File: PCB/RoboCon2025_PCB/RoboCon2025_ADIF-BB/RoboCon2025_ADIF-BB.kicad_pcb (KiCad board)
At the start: 2 copper layers, 47 x 72 mm, 27 parts, among them J1 Conn_01x05, J2 Conn_01x09, J3 Conn_01x09, J4 S2B-XH-A, J6 S3B-XH-A, J7 S2B-XH-A, J8 S2B-XH-A, J9 S3B-XH-A, U1 PCM5102A, U3 TBD62083AFNG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

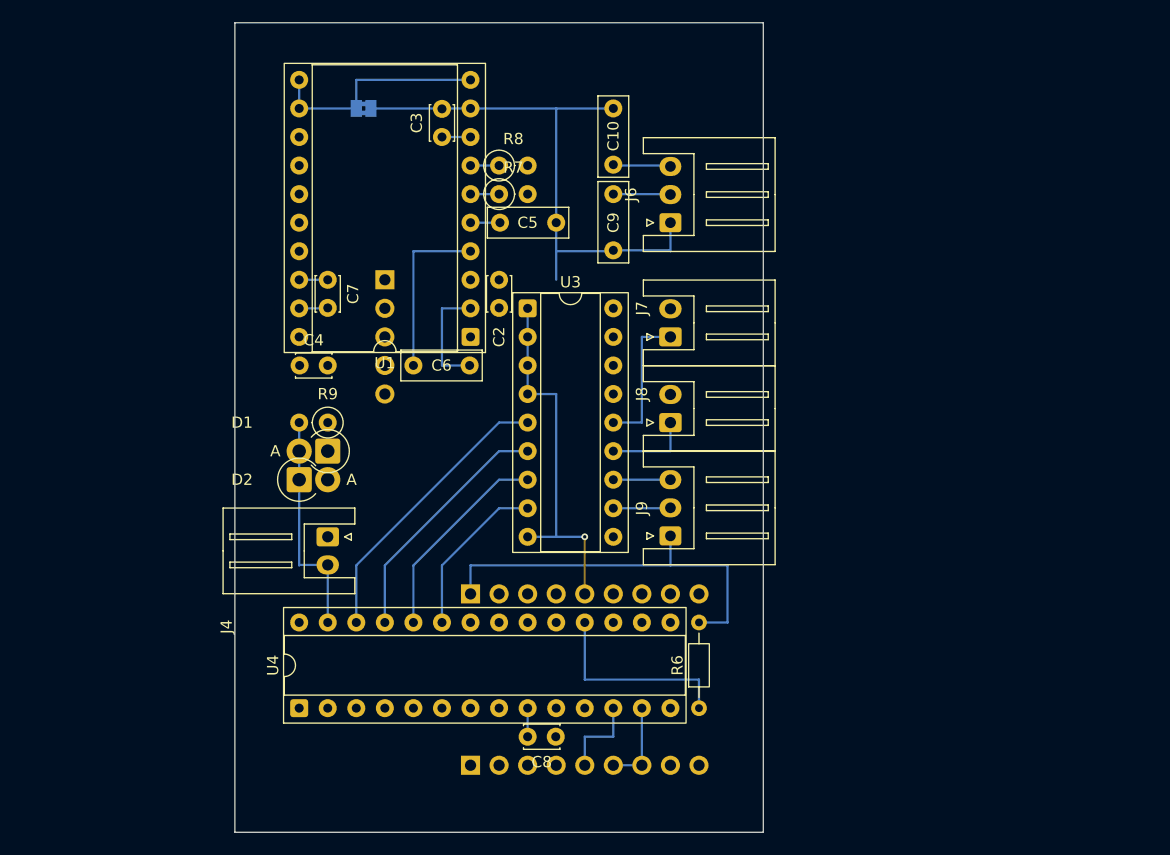
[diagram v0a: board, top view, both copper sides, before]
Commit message: [PCB] update: BB基板のパターン引いた(未配線あり)
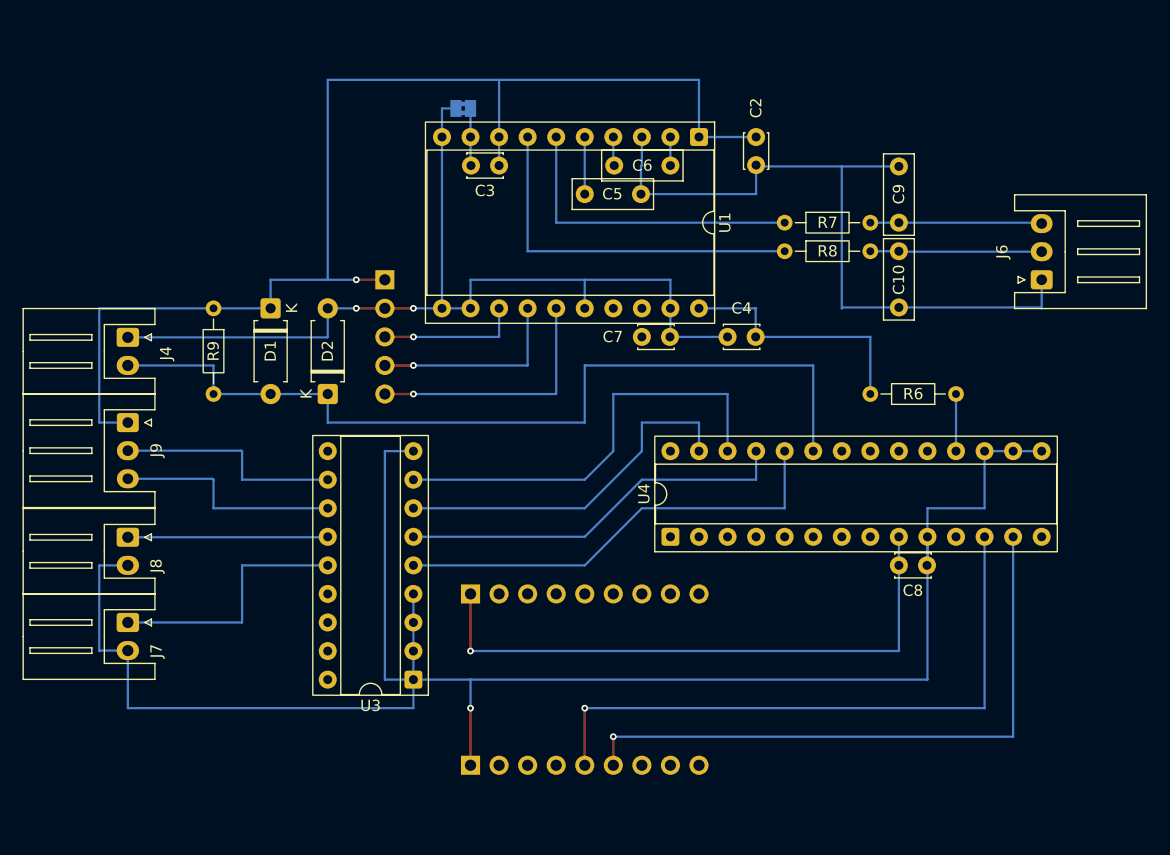
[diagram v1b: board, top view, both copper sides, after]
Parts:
- D1, D2: footprint Diode_THT:D_DO-15_P2.54mm_Vertical_AnodeUp -> Diode_THT:D_A-405_P7.62mm_Horizontal
- R7, R8, R9: footprint Resistor_THT:R_Axial_DIN0207_L6.3mm_D2.5mm_P2.54mm_Vertical -> Resistor_THT:R_Axial_DIN0204_L3.6mm_D1.6mm_P7.62mm_Horizontal
- moved J7 54.5 mm to (101.6, 96.5), turned to -90 degrees
- moved J8 49.3 mm to (101.6, 88.9), turned to -90 degrees
- moved J9 49.3 mm to (101.6, 78.7), turned to -90 degrees
- moved C4 40.6 mm to (157.4, 71.1), turned to 180 degrees
- moved C8 36.4 mm to (172.7, 91.4)
- moved U4 36.4 mm to (149.9, 88.9)
- moved R6 36.1 mm to (175.3, 76.2), turned to 180 degrees
- moved U3 34.5 mm to (127.0, 101.6), turned to 180 degrees
- moved J6 33.4 mm to (182.9, 66.0)
- moved C7 28.4 mm to (147.3, 71.1), turned to 0 degrees
- moved C2 27.5 mm to (157.5, 53.3), turned to -90 degrees
- moved U1 27.0 mm to (152.4, 53.3), turned to -90 degrees
- moved C10 26.5 mm to (170.2, 63.5), turned to -90 degrees
- moved R8 26.5 mm to (160.0, 63.5)
- moved C9 25.5 mm to (170.2, 61.0), turned to 90 degrees
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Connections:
- J2 pad 7: /EXT_3SDA -> unconnected-(J2-Pin_7-Pad7)
- J3 pad 5: GND -> unconnected-(J3-Pin_5-Pad5)
- J6 pad 2: /AUDIO_OUT_L -> /AUDIO_OUT_R
- J6 pad 3: /AUDIO_OUT_R -> /AUDIO_OUT_L
- U4 pad 23: Net-(U3-I8) -> ACT_N
- U4 pad 24: Net-(U3-I7) -> Net-(U3-I5)
- U4 pad 26: Net-(U3-I5) -> Net-(U3-I8)
- U4 pad 27: ACT_N -> Net-(U3-I7)
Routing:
- net GND: track 55.9 -> 250.3 mm, vias 1 -> 3
- net +3V3: track 40.7 -> 185.5 mm, vias 0 -> 2
- net ACT_N: track 20.4 -> 78.7 mm
- net /EXT_3SDA: track 7.62 -> 55.9 mm, vias 0 -> 1
- net /EXT_3SCL: track 7.62 -> 55.9 mm, vias 0 -> 1
- net Net-(U1-OUTR): track 2.54 -> 33.0 mm
- net Net-(U1-OUTL): track 2.54 -> 27.9 mm
- net Net-(U3-I8): track 14.8 -> 39.2 mm
- net /I2S_LRCK: track 0.00 -> 22.9 mm, vias 0 -> 1
- net GNDA: track 49.9 -> 68.8 mm
- net /I2S_DIN: track 0.00 -> 17.8 mm, vias 0 -> 1
- net Net-(J9-Pin_3): track 5.08 -> 20.4 mm
- net Net-(J9-Pin_2): track 5.10 -> 20.3 mm
- net Net-(U3-I5): track 25.6 -> 40.2 mm
- net Net-(U3-I7): track 18.4 -> 32.6 mm
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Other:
- board outline removed

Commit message: [PCB] update: 配線完了！
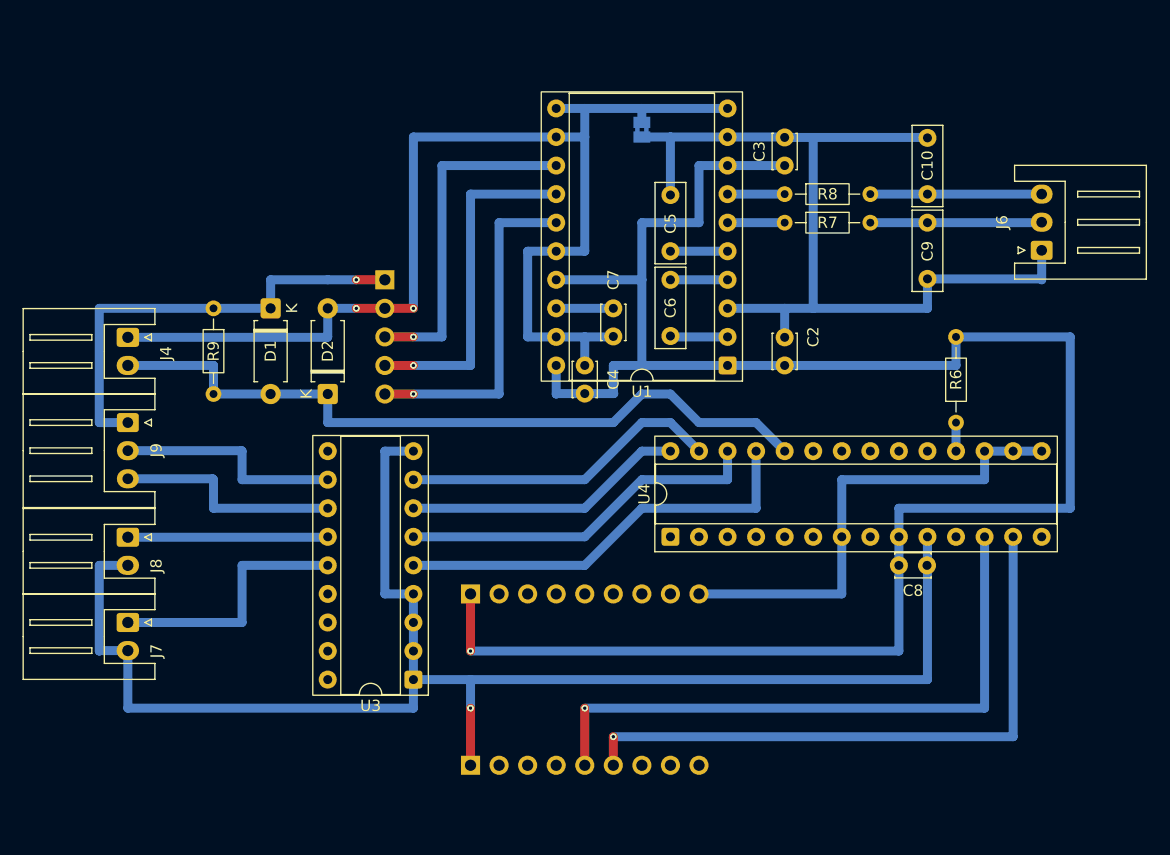
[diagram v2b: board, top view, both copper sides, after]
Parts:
- moved C3 25.4 mm to (160.0, 55.9), turned to 90 degrees
- moved C2 20.5 mm to (160.0, 73.7), turned to 90 degrees
- moved U1 20.5 mm to (154.9, 73.7), turned to 180 degrees
- moved C4 16.0 mm to (142.2, 76.2), turned to 90 degrees
- moved JP1 16.0 mm to (147.3, 52.7), turned to -90 degrees
- moved C6 11.3 mm to (149.9, 66.0), turned to -90 degrees
- moved C5 9.16 mm to (149.9, 63.5), turned to 90 degrees
- moved C10 5.68 mm to (172.7, 58.4), turned to 90 degrees
- moved R8 5.08 mm to (160.0, 58.4)
- moved C7 3.59 mm to (144.8, 68.6), turned to -90 degrees
- moved J6 2.62 mm to (182.9, 63.4)
- moved C9 2.54 mm to (172.7, 61.0), turned to -90 degrees
- moved R6 2.54 mm to (175.3, 78.7), turned to 90 degrees
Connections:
- J2 pad 9: GND -> unconnected-(J2-Pin_9-Pad9)
- J3 pad 9: unconnected-(J3-Pin_9-Pad9) -> GND
- J6 pad 2: /AUDIO_OUT_R -> /AUDIO_OUT_L
- J6 pad 3: /AUDIO_OUT_L -> /AUDIO_OUT_R
- U4 pad 23: ACT_N -> unconnected-(U4-GPA2-Pad23)
- U4 pad 24: Net-(U3-I5) -> ACT_N
- U4 pad 25: Net-(U3-I6) -> Net-(U3-I5)
- U4 pad 26: Net-(U3-I8) -> Net-(U3-I6)
- U4 pad 27: Net-(U3-I7) -> Net-(U3-I8)
- U4 pad 28: unconnected-(U4-GPA7-Pad28) -> Net-(U3-I7)
- U4 pad 7: unconnected-(U4-GPB6-Pad7) -> GND
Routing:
- net GND: track 250.3 -> 293.5 mm
- net +3V3: track 185.5 -> 218.5 mm
- net Net-(U1-OUTR): track 33.0 -> 5.08 mm
- net Net-(U1-OUTL): track 27.9 -> 5.08 mm
- net /I2S_BCLK: track 12.7 -> 30.5 mm
- net GNDA: track 68.8 -> 81.6 mm
- net /I2S_DIN: track 17.8 -> 30.5 mm
- net ACT_N: track 78.7 -> 66.7 mm
- net Net-(U3-I8): track 39.2 -> 28.6 mm
- net Net-(U3-I7): track 32.6 -> 25.0 mm
- net /I2S_LRCK: track 22.9 -> 30.5 mm
- net Net-(U1-LDOO): track 0.00 -> 5.08 mm
- net Net-(U1-CAPP): track 2.54 -> 5.11 mm
- net Net-(U3-I5): track 40.2 -> 37.7 mm
- net Net-(U4-~{RESET}): track 5.08 -> 2.54 mm
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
